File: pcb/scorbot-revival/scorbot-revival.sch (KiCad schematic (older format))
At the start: 4 parts, among them J1 DB-50, J2 Raspberry_Pi_2_3, U1 L293D, U2 PIC18F2431-E_SP

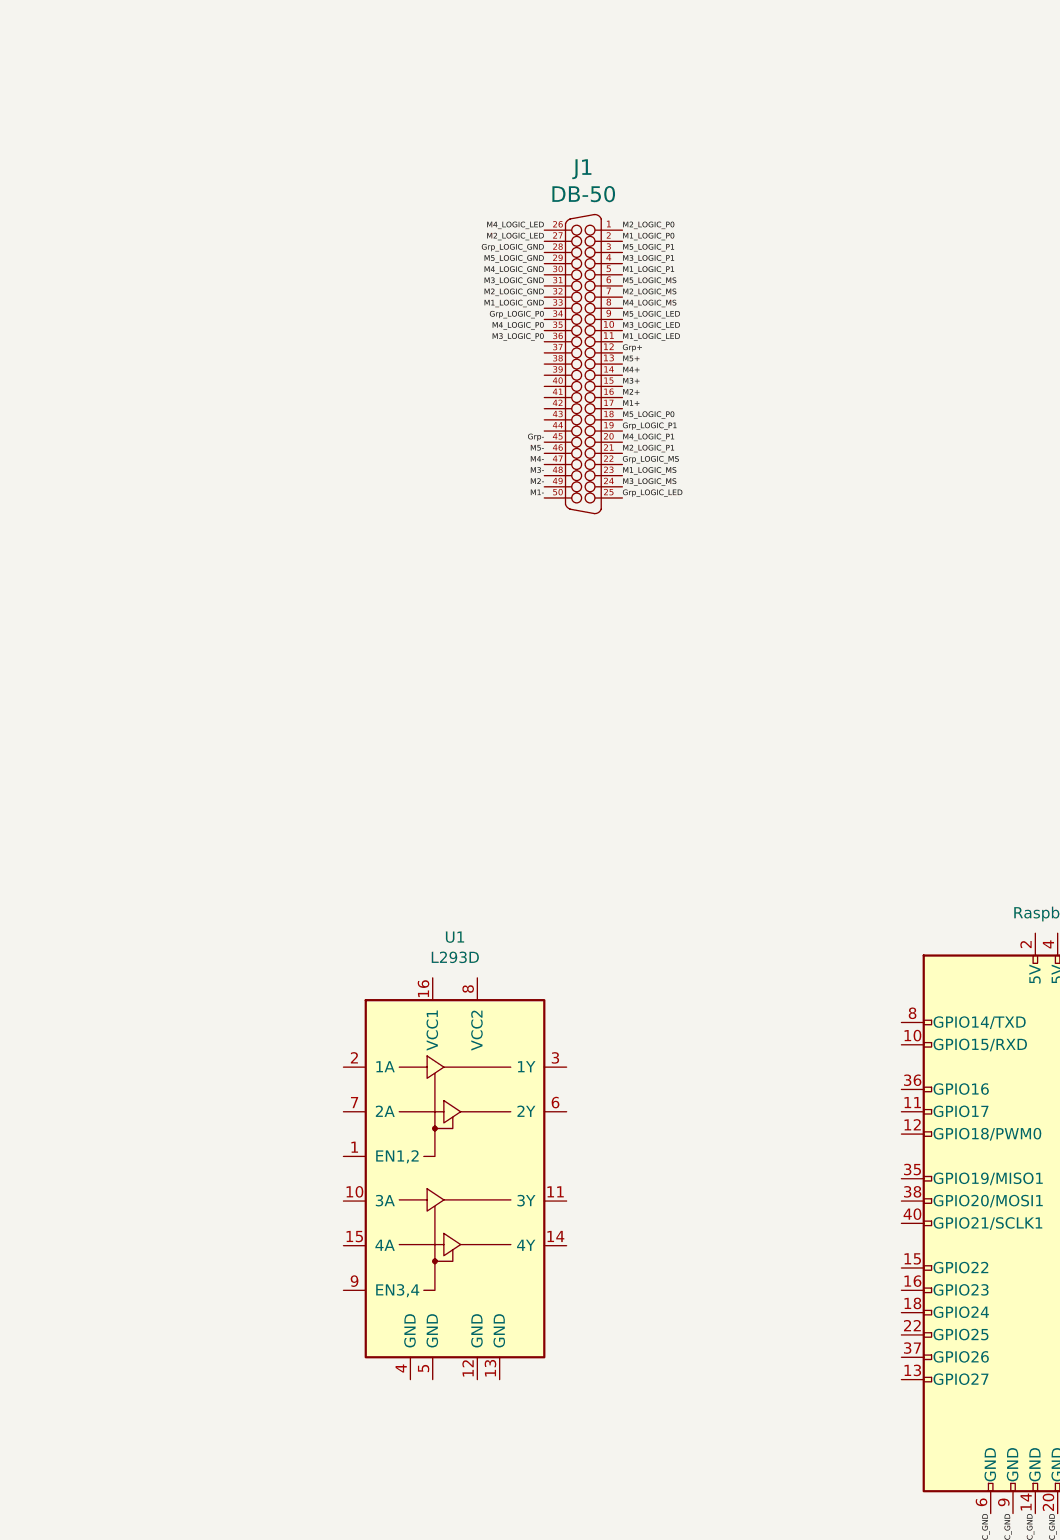
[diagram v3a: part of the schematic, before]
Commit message: [pcb] update schematic connections
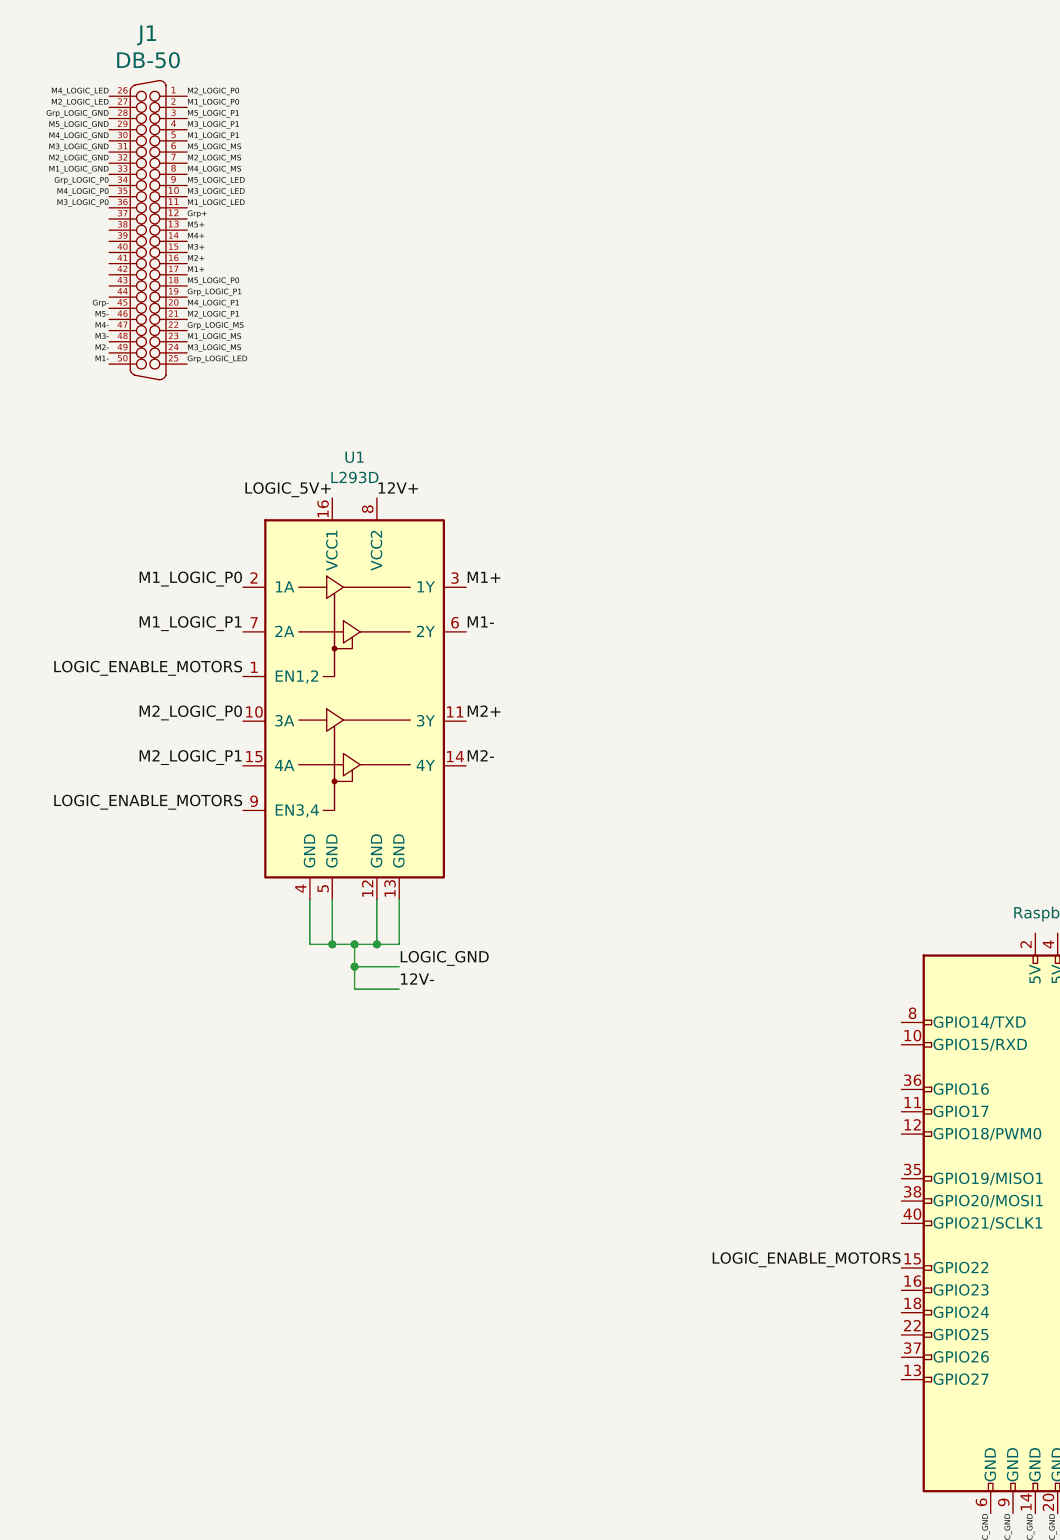
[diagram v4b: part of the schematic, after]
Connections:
- net M1+: now also U1.3 (1Y)
- net M1-: now also U1.6 (2Y)
- net M1_LOGIC_P0: now also U1.2 (1A)
- net M1_LOGIC_P1: now also U1.7 (2A)
- net M2+: now also U1.11 (3Y)
- net M2-: now also U1.14 (4Y)
- net M2_LOGIC_P0: now also U1.10 (3A)
- net M2_LOGIC_P1: now also U1.15 (4A)
- net LOGIC_ENABLE_MOTORS: now reaches U1.1 (EN1,2)
- net LOGIC_ENABLE_MOTORS: now also J2.15 (GPIO22), U1.9 (EN3,4)
- net 12V-: now reaches U1.12 (GND)
- net 12V-: now also U1.13 (GND), U1.4 (GND), U1.5 (GND)
- net LOGIC_5V+: now reaches U1.16 (VCC1)
- net 12V+: now reaches U1.8 (VCC2)
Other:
- moved on the sheet: J1, U1
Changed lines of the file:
@@
 L Driver_Motor:L293D U1
 U 1 1 5DE0ADB2
-P 2450 5850
-F 0 "U1" H 2450 7031 50  0000 C CNN
-F 1 "L293D" H 2450 6940 50  0000 C CNN
-F 2 "Package_DIP:DIP-16_W7.62mm" H 2700 5100 50  0001 L CNN
-F 3 "http://www.ti.com/lit/ds/symlink/l293.pdf" H 2150 6550 50  0001 C CNN
-	1    2450 5850
+P 2000 3700
+F 0 "U1" H 2000 4881 50  0000 C CNN
+F 1 "L293D" H 2000 4790 50  0000 C CNN
+F 2 "Package_DIP:DIP-16_W7.62mm" H 2250 2950 50  0001 L CNN
+F 3 "http://www.ti.com/lit/ds/symlink/l293.pdf" H 1700 4400 50  0001 C CNN
+	1    2000 3700
 	1    0    0    -1
 $EndComp
@@
 L smisioto_connectors:DB-50 J1
 U 1 1 5DE13F75
-P 3025 2100
-F 0 "J1" H 3025 2980 70  0000 C CNN
-F 1 "DB-50" H 3025 2859 70  0000 C CNN
-F 2 "LibraryLoader:09665526612" H 3025 2100 60  0001 C CNN
-F 3 "" H 3025 2100 60  0000 C CNN
-	1    3025 2100
-	1    0    0    -1
-$EndComp
-Text Label 2850 2700 2    25   ~ 0
+P 1075 1500
+F 0 "J1" H 1075 2380 70  0000 C CNN
+F 1 "DB-50" H 1075 2259 70  0000 C CNN
+F 2 "LibraryLoader:09665526612" H 1075 1500 60  0001 C CNN
+F 3 "" H 1075 1500 60  0000 C CNN
+	1    1075 1500
+	1    0    0    -1
+$EndComp
+Text Label 900  2100 2    25   ~ 0
 M1-
-Text Label 2850 2650 2    25   ~ 0
+Text Label 900  2050 2    25   ~ 0
 M2-
-Text Label 2850 2600 2    25   ~ 0
+Text Label 900  2000 2    25   ~ 0
 M3-
-Text Label 2850 2550 2    25   ~ 0
+Text Label 900  1950 2    25   ~ 0
 M4-
-Text Label 2850 2500 2    25   ~ 0
+Text Label 900  1900 2    25   ~ 0
 M5-
-Text Label 2850 2450 2    25   ~ 0
+Text Label 900  1850 2    25   ~ 0
 Grp-
-Text Label 3200 2300 0    25   ~ 0
+Text Label 1250 1700 0    25   ~ 0
 M1+
-Text Label 3200 2250 0    25   ~ 0
+Text Label 1250 1650 0    25   ~ 0
 M2+
-Text Label 3200 2200 0    25   ~ 0
+Text Label 1250 1600 0    25   ~ 0
 M3+
-Text Label 3200 2150 0    25   ~ 0
+Text Label 1250 1550 0    25   ~ 0
 M4+
-Text Label 3200 2100 0    25   ~ 0
+Text Label 1250 1500 0    25   ~ 0
 M5+
-Text Label 3200 2050 0    25   ~ 0
+Text Label 1250 1450 0    25   ~ 0
 Grp+
-Text Label 2850 1850 2    25   ~ 0
+Text Label 900  1250 2    25   ~ 0
 M1_LOGIC_GND
-Text Label 2850 1800 2    25   ~ 0
+Text Label 900  1200 2    25   ~ 0
 M2_LOGIC_GND
-Text Label 2850 1750 2    25   ~ 0
+Text Label 900  1150 2    25   ~ 0
 M3_LOGIC_GND
-Text Label 2850 1700 2    25   ~ 0
+Text Label 900  1100 2    25   ~ 0
 M4_LOGIC_GND
-Text Label 2850 1650 2    25   ~ 0
+Text Label 900  1050 2    25   ~ 0
 M5_LOGIC_GND
-Text Label 2850 1600 2    25   ~ 0
+Text Label 900  1000 2    25   ~ 0
 Grp_LOGIC_GND
-Text Label 3200 2000 0    25   ~ 0
+Text Label 1250 1400 0    25   ~ 0
 M1_LOGIC_LED
-Text Label 2850 1550 2    25   ~ 0
+Text Label 900  950  2    25   ~ 0
 M2_LOGIC_LED
-Text Label 3200 1950 0    25   ~ 0
+Text Label 1250 1350 0    25   ~ 0
 M3_LOGIC_LED
-Text Label 2850 1500 2    25   ~ 0
+Text Label 900  900  2    25   ~ 0
 M4_LOGIC_LED
-Text Label 3200 1900 0    25   ~ 0
+Text Label 1250 1300 0    25   ~ 0
 M5_LOGIC_LED
-Text Label 3200 2700 0    25   ~ 0
+Text Label 1250 2100 0    25   ~ 0
 Grp_LOGIC_LED
-Text Label 3200 1700 0    25   ~ 0
+Text Label 1250 1100 0    25   ~ 0
 M1_LOGIC_P1
-Text Label 3200 2500 0    25   ~ 0
+Text Label 1250 1900 0    25   ~ 0
 M2_LOGIC_P1
-Text Label 3200 1650 0    25   ~ 0
+Text Label 1250 1050 0    25   ~ 0
 M3_LOGIC_P1
-Text Label 3200 2450 0    25   ~ 0
+Text Label 1250 1850 0    25   ~ 0
 M4_LOGIC_P1
-Text Label 3200 1600 0    25   ~ 0
+Text Label 1250 1000 0    25   ~ 0
 M5_LOGIC_P1
-Text Label 3200 2400 0    25   ~ 0
+Text Label 1250 1800 0    25   ~ 0
 Grp_LOGIC_P1
-Text Label 3200 1550 0    25   ~ 0
+Text Label 1250 950  0    25   ~ 0
 M1_LOGIC_P0
-Text Label 3200 1500 0    25   ~ 0
+Text Label 1250 900  0    25   ~ 0
 M2_LOGIC_P0
-Text Label 2850 2000 2    25   ~ 0
+Text Label 900  1400 2    25   ~ 0
 M3_LOGIC_P0
-Text Label 2850 1950 2    25   ~ 0
+Text Label 900  1350 2    25   ~ 0
 M4_LOGIC_P0
-Text Label 3200 2350 0    25   ~ 0
+Text Label 1250 1750 0    25   ~ 0
 M5_LOGIC_P0
-Text Label 2850 1900 2    25   ~ 0
+Text Label 900  1300 2    25   ~ 0
 Grp_LOGIC_P0
-Text Label 3200 2600 0    25   ~ 0
+Text Label 1250 2000 0    25   ~ 0
 M1_LOGIC_MS
-Text Label 3200 1800 0    25   ~ 0
+Text Label 1250 1200 0    25   ~ 0
 M2_LOGIC_MS
-Text Label 3200 2650 0    25   ~ 0
+Text Label 1250 2050 0    25   ~ 0
 M3_LOGIC_MS
-Text Label 3200 1850 0    25   ~ 0
+Text Label 1250 1250 0    25   ~ 0
 M4_LOGIC_MS
-Text Label 3200 1750 0    25   ~ 0
+Text Label 1250 1150 0    25   ~ 0
 M5_LOGIC_MS
-Text Label 3200 2550 0    25   ~ 0
+Text Label 1250 1950 0    25   ~ 0
 Grp_LOGIC_MS
 Text Label 4850 7250 3    25   ~ 0
@@
 	1    0    0    -1
 $EndComp
+Text Label 1900 2700 2    50   ~ 0
+LOGIC_5V+
+Text Label 2100 2700 0    50   ~ 0
+12V+
+Wire Wire Line
+	1800 4500 1800 4700
+Wire Wire Line
+	1800 4700 1900 4700
+Wire Wire Line
+	1900 4500 1900 4700
+Connection ~ 1900 4700
+Wire Wire Line
+	1900 4700 2000 4700
+Wire Wire Line
+	2100 4500 2100 4700
+Connection ~ 2100 4700
+Wire Wire Line
+	2100 4700 2200 4700
+Wire Wire Line
+	2200 4500 2200 4700
+Wire Wire Line
+	2000 4700 2000 4800
+Connection ~ 2000 4700
+Wire Wire Line
+	2000 4700 2100 4700
+Text Label 2200 4800 0    50   ~ 0
+LOGIC_GND
+Text Label 2200 4900 0    50   ~ 0
+12V-
+Wire Wire Line
+	2000 4800 2200 4800
+Wire Wire Line
+	2000 4800 2000 4900
+Wire Wire Line
+	2000 4900 2200 4900
+Connection ~ 2000 4800
+Text Label 2500 3100 0    50   ~ 0
+M1+
+Text Label 2500 3300 0    50   ~ 0
+M1-
+Text Label 2500 3700 0    50   ~ 0
+M2+
+Text Label 2500 3900 0    50   ~ 0
+M2-
+Text Label 1500 3100 2    50   ~ 0
+M1_LOGIC_P0
+Text Label 1500 3300 2    50   ~ 0
+M1_LOGIC_P1
+Text Label 1500 3700 2    50   ~ 0
+M2_LOGIC_P0
+Text Label 1500 3900 2    50   ~ 0
+M2_LOGIC_P1
+Text Label 1500 3500 2    50   ~ 0
+LOGIC_ENABLE_MOTORS
+Text Label 1500 4100 2    50   ~ 0
+LOGIC_ENABLE_MOTORS
+Text Label 4450 6150 2    50   ~ 0
+LOGIC_ENABLE_MOTORS
 $EndSCHEMATC
